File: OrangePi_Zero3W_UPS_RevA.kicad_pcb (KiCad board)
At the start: 4 copper layers, 65 x 32 mm, 74 parts, among them J1 ORANGE_PI_ZERO_3W_HEADER, J2 BATTERY_1S_PROTECTED_NTC, J3 USB_C_POWER_INPUT, Q1 STL9P3LLH6, SW1 POWER / QON, U1 MAX17048G_T10, U2 BQ25895RTWR, U3 STUSB4500LQTR, U4 USBLC6-2SC6, U5 TPS61088RHLR, U6 TPS259470ARPWR

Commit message: Phase 6B.2B5: finalize placement clearance and assembly review
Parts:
- moved C26 0.20 mm to (114.0, 87.5)
- moved C8 0.20 mm to (73.0, 82.8)
- moved Q1 0.20 mm to (76.1, 82.0)
- moved R11 0.20 mm to (76.2, 90.1)
- moved R14 0.20 mm to (106.9, 95.8)
- moved C29 0.15 mm to (117.8, 90.7)
- moved R12 0.15 mm to (77.9, 90.1)
- moved U6 0.15 mm to (117.2, 87.5)
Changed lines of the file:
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@@
 	(footprint "Capacitor_SMD:C_0603_1608Metric"
 		(layer "F.Cu")
-		(at 73.200 82.800 90)
+		(at 73.000 82.800 90)
 		(descr "Capacitor SMD 0603 (1608 Metric), square (rectangular) end terminal, IPC-7351 nominal, (Body size source: IPC-SM-782 page 76, https://www.pcb-3d.com/wordpress/wp-content/uploads/ipc-sm-782a_amendment_1_and_2.pdf), generated with kicad-footprint-generator")
 		(tags "capacitor")
@@
 	(footprint "Resistor_SMD:R_0603_1608Metric"
 		(layer "F.Cu")
-		(at 76.000 90.100 90)
+		(at 76.200 90.100 90)
 		(descr "Resistor SMD 0603 (1608 Metric), square (rectangular) end terminal, IPC-7351 nominal, (Body size source: IPC-SM-782 page 72, https://www.pcb-3d.com/wordpress/wp-content/uploads/ipc-sm-782a_amendment_1_and_2.pdf), generated with kicad-footprint-generator")
 		(tags "resistor")
@@
 	(footprint "Resistor_SMD:R_0603_1608Metric"
 		(layer "F.Cu")
-		(at 77.750 90.100 90)
+		(at 77.900 90.100 90)
 		(descr "Resistor SMD 0603 (1608 Metric), square (rectangular) end terminal, IPC-7351 nominal, (Body size source: IPC-SM-782 page 72, https://www.pcb-3d.com/wordpress/wp-content/uploads/ipc-sm-782a_amendment_1_and_2.pdf), generated with kicad-footprint-generator")
 		(tags "resistor")
@@
 	(footprint "Resistor_SMD:R_0603_1608Metric"
 		(layer "F.Cu")
-		(at 106.900 96.000 -90)
+		(at 106.900 95.800 -90)
 		(descr "Resistor SMD 0603 (1608 Metric), square (rectangular) end terminal, IPC-7351 nominal, (Body size source: IPC-SM-782 page 72, https://www.pcb-3d.com/wordpress/wp-content/uploads/ipc-sm-782a_amendment_1_and_2.pdf), generated with kicad-footprint-generator")
 		(tags "resistor")
@@
 	(footprint "Capacitor_SMD:C_0603_1608Metric"
 		(layer "F.Cu")
-		(at 117.900 90.700 90)
+		(at 117.750 90.700 90)
 		(descr "Capacitor SMD 0603 (1608 Metric), square (rectangular) end terminal, IPC-7351 nominal, (Body size source: IPC-SM-782 page 76, https://www.pcb-3d.com/wordpress/wp-content/uploads/ipc-sm-782a_amendment_1_and_2.pdf), generated with kicad-footprint-generator")
 		(tags "capacitor")
@@
 	(footprint "STL9P3LLH6:TRANS_STL9P3LLH6"
 		(layer "F.Cu")
-		(at 76.300 82.000)
+		(at 76.100 82.000)
 		(property "Reference" "Q1"
 			(at 0 -2.45 0)
@@
 	(footprint "TPS25947_fixed:TPS259470ARPWR_RPW0010A"
 		(layer "F.Cu")
-		(at 117.350 87.500)
+		(at 117.200 87.500)
 		(descr "Texas Instruments RPW0010A VQFN-HR-10, 2.0x2.0mm, 0.45mm pitch; corner terminals use duplicate same-number pad primitives to form the recommended L-shaped lands")
 		(tags "TPS25947 RPW0010A VQFN-HR-10 eFuse")
@@
 	(footprint "Capacitor_SMD:C_0603_1608Metric"
 		(layer "F.Cu")
-		(at 114.200 87.500)
+		(at 114.000 87.500)
 		(descr "Capacitor SMD 0603 (1608 Metric), square (rectangular) end terminal, IPC-7351 nominal, (Body size source: IPC-SM-782 page 76, https://www.pcb-3d.com/wordpress/wp-content/uploads/ipc-sm-782a_amendment_1_and_2.pdf), generated with kicad-footprint-generator")
 		(tags "capacitor")

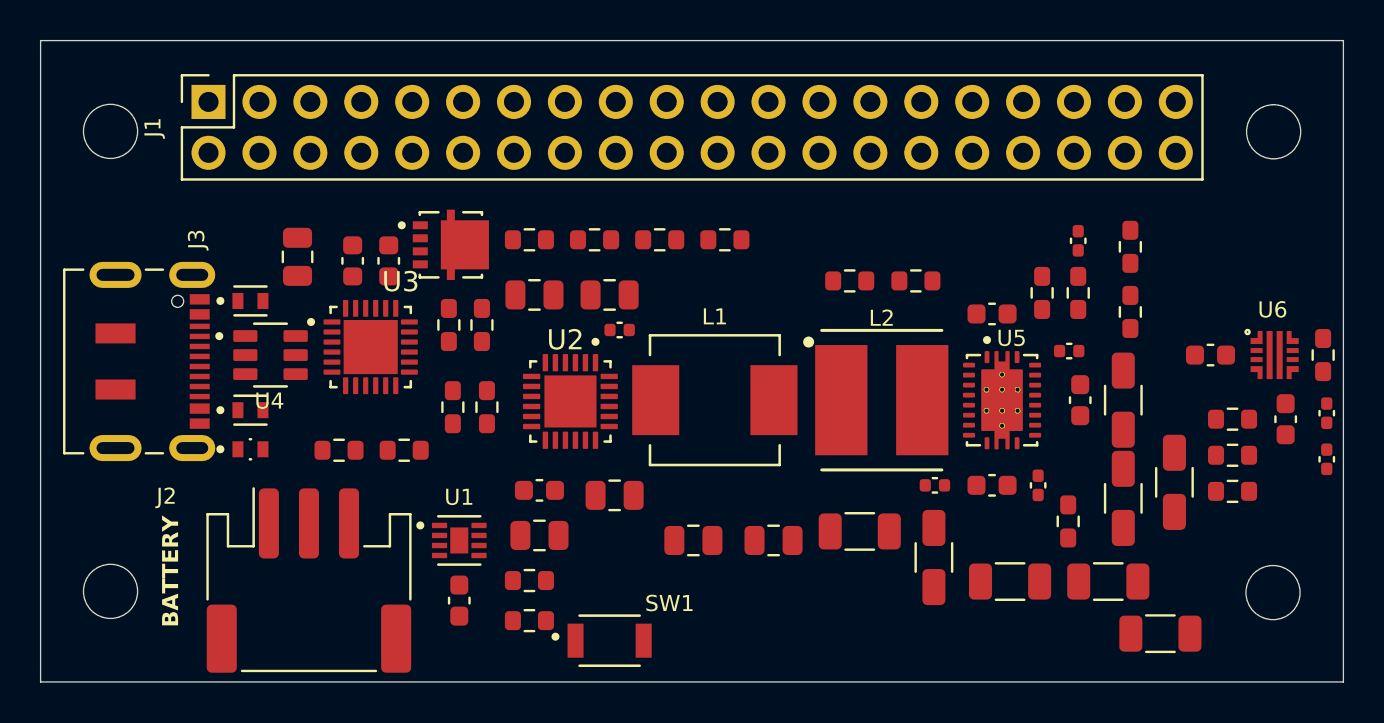
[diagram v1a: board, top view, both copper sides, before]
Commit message: Phase 6B.2B2 — TPS61088, Phase 6B.2B3 — TPS25947, Phase 6B.2B4 — USB-C/STUSB4500L/ESD, Phase 6B.2B5 — final placement review
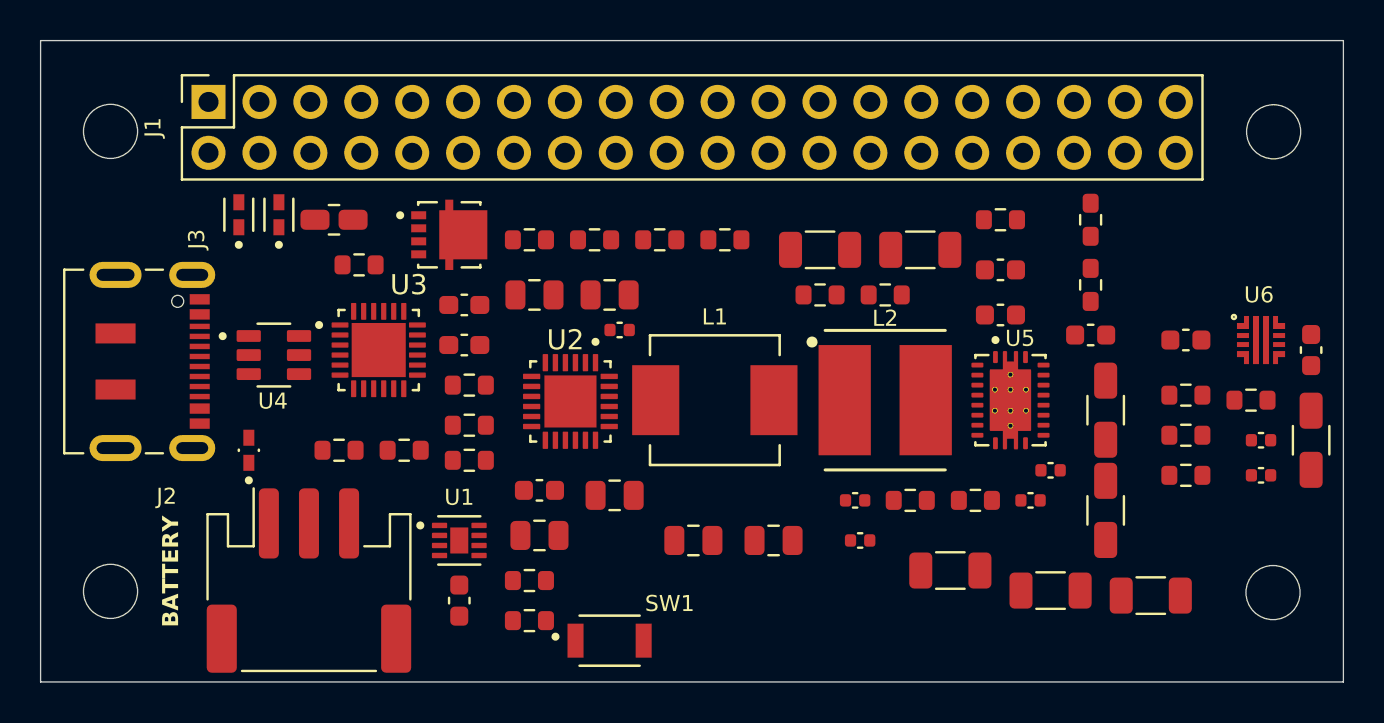
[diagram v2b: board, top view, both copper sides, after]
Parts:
- moved C15 15.4 mm to (99.5, 82.2), turned to 0 degrees
- moved R14 14.5 mm to (97.8, 84.5), turned to 0 degrees
- moved C14 14.2 mm to (94.5, 82.2)
- moved C24 13.2 mm to (105.0, 94.8), turned to 0 degrees
- moved R18 12.3 mm to (99.0, 94.8), turned to 0 degrees
- moved R19 11.6 mm to (102.3, 94.8), turned to 0 degrees
- moved C13 10.8 mm to (103.5, 83.2)
- moved D2 9.85 mm to (67.5, 80.5), turned to 90 degrees
- moved C23 9.30 mm to (96.5, 96.8), turned to 0 degrees
- moved C30 7.14 mm to (119.0, 91.8)
- moved C9 6.98 mm to (76.8, 87.0), turned to 0 degrees
- moved C25 6.02 mm to (106.0, 93.2), turned to 0 degrees
- moved R10 5.39 mm to (71.5, 83.0), turned to 0 degrees
- moved R17 5.21 mm to (103.5, 80.8)
- moved C8 4.36 mm to (76.8, 85.0), turned to 0 degrees
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
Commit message: Phase 6C.1B — Node SYS_BAT lokal
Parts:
- moved C4 2.46 mm to (90.2, 95.2), turned to -90 degrees
- moved C3 1.56 mm to (88.0, 95.2), turned to -90 degrees
- moved C7 0.50 mm to (84.3, 95.0)
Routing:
- net /SYS_BAT: track 0.00 -> 18.9 mm
- net /SW_CHG: track 0.00 -> 4.14 mm
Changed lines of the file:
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@@
 	(footprint "Capacitor_SMD:C_0805_2012Metric"
 		(layer "F.Cu")
-		(at 84.27 94.5)
+		(at 84.27 95)
 		(descr "Capacitor SMD 0805 (2012 Metric), square (rectangular) end terminal, IPC-7351 nominal, (Body size source: IPC-SM-782 page 76, https://www.pcb-3d.com/wordpress/wp-content/uploads/ipc-sm-782a_amendment_1_and_2.pdf, https://docs.google.com/spreadsheets/d/1BsfQQcO9C6DZCsRaXUlFlo91Tg2WpOkGARC1WS5S8t0/edit?usp=sharing), generated with kicad-footprint-generator")
 		(tags "capacitor")
@@
 	(footprint "Capacitor_SMD:C_0805_2012Metric"
 		(layer "F.Cu")
-		(at 92.2 96.75)
+		(at 90.25 95.25 -90)
 		(descr "Capacitor SMD 0805 (2012 Metric), square (rectangular) end terminal, IPC-7351 nominal, (Body size source: IPC-SM-782 page 76, https://www.pcb-3d.com/wordpress/wp-content/uploads/ipc-sm-782a_amendment_1_and_2.pdf, https://docs.google.com/spreadsheets/d/1BsfQQcO9C6DZCsRaXUlFlo91Tg2WpOkGARC1WS5S8t0/edit?usp=sharing), generated with kicad-footprint-generator")
 		(tags "capacitor")
 		(property "Reference" "C4"
-			(at 0 -1.5 0)
+			(at 0 -1.5 90)
 			(layer "F.SilkS")
 			(hide yes)
@@
 		)
 		(property "Value" "10uF"
-			(at 0 1.68 0)
+			(at 0 1.68 90)
 			(layer "F.Fab")
 			(effects
@@
 		)
 		(property "Datasheet" "~"
-			(at 0 0 0)
+			(at 0 0 90)
 			(layer "F.Fab")
 			(hide yes)
@@
 		)
 		(property "Description" "Unpolarized capacitor"
-			(at 0 0 0)
+			(at 0 0 90)
 			(layer "F.Fab")
 			(hide yes)
@@
 		(attr smd)
 		(fp_line
-			(start -0.261252 -0.735)
-			(end 0.261252 -0.735)
+			(start -0.261252 0.735)
+			(end 0.261252 0.735)
 			(stroke
 				(width 0.12)
@@
 		)
 		(fp_line
-			(start -0.261252 0.735)
-			(end 0.261252 0.735)
+			(start -0.261252 -0.735)
+			(end 0.261252 -0.735)
 			(stroke
 				(width 0.12)
@@
 		)
 		(fp_line
-			(start -1.7 -0.98)
-			(end 1.7 -0.98)
+			(start -1.7 0.98)
+			(end -1.7 -0.98)
 			(stroke
 				(width 0.05)
@@
 		)
 		(fp_line
-			(start -1.7 0.98)
-			(end -1.7 -0.98)
+			(start 1.7 0.98)
+			(end -1.7 0.98)
 			(stroke
 				(width 0.05)
@@
 		)
 		(fp_line
-			(start 1.7 -0.98)
-			(end 1.7 0.98)
+			(start -1.7 -0.98)
+			(end 1.7 -0.98)
 			(stroke
 				(width 0.05)
@@
 		)
 		(fp_line
-			(start 1.7 0.98)
-			(end -1.7 0.98)
+			(start 1.7 -0.98)
+			(end 1.7 0.98)
 			(stroke
 				(width 0.05)
@@
 		)
 		(fp_line
-			(start -1 -0.625)
-			(end 1 -0.625)
+			(start -1 0.625)
+			(end -1 -0.625)
 			(stroke
 				(width 0.1)
@@
 		)
 		(fp_line
-			(start -1 0.625)
-			(end -1 -0.625)
+			(start 1 0.625)
+			(end -1 0.625)
 			(stroke
 				(width 0.1)
@@
 		)
 		(fp_line
-			(start 1 -0.625)
-			(end 1 0.625)
+			(start -1 -0.625)
+			(end 1 -0.625)
 			(stroke
 				(width 0.1)
@@
 		)
 		(fp_line
-			(start 1 0.625)
-			(end -1 0.625)
+			(start 1 -0.625)
+			(end 1 0.625)
 			(stroke
 				(width 0.1)
@@
 		)
 		(fp_text user "${REFERENCE}"
-			(at 0 0 0)
+			(at 0 0 90)
 			(layer "F.Fab")
 			(effects
@@
 		)
 		(pad "1" smd roundrect
-			(at -0.95 0)
+			(at -0.95 0 270)
 			(size 1 1.45)
 			(layers "F.Cu" "F.Mask" "F.Paste")
@@
 		)
 		(pad "2" smd roundrect
-			(at 0.95 0)
+			(at 0.95 0 270)
 			(size 1 1.45)
 			(layers "F.Cu" "F.Mask" "F.Paste")
@@
 	(footprint "Capacitor_SMD:C_0805_2012Metric"
 		(layer "F.Cu")
-		(at 88.2 96.75)
+		(at 88.05 95.2 -90)
 		(descr "Capacitor SMD 0805 (2012 Metric), square (rectangular) end terminal, IPC-7351 nominal, (Body size source: IPC-SM-782 page 76, https://www.pcb-3d.com/wordpress/wp-content/uploads/ipc-sm-782a_amendment_1_and_2.pdf, https://docs.google.com/spreadsheets/d/1BsfQQcO9C6DZCsRaXUlFlo91Tg2WpOkGARC1WS5S8t0/edit?usp=sharing), generated with kicad-footprint-generator")
 		(tags "capacitor")
 		(property "Reference" "C3"
-			(at 0 -1.5 0)
+			(at 0 -1.5 90)
 			(layer "F.SilkS")
 			(hide yes)
@@
 		)
 		(property "Value" "10uF"
-			(at 0 1.68 0)
+			(at 0 1.68 90)
 			(layer "F.Fab")
 			(effects
@@
 		)
 		(property "Datasheet" "~"
-			(at 0 0 0)
+			(at 0 0 90)
 			(layer "F.Fab")
 			(hide yes)
@@
 		)
 		(property "Description" "Unpolarized capacitor"
-			(at 0 0 0)
+			(at 0 0 90)
 			(layer "F.Fab")
 			(hide yes)
@@
 		(attr smd)
 		(fp_line
-			(start -0.261252 -0.735)
-			(end 0.261252 -0.735)
+			(start -0.261252 0.735)
+			(end 0.261252 0.735)
 			(stroke
 				(width 0.12)
@@
 		)
 		(fp_line
-			(start -0.261252 0.735)
-			(end 0.261252 0.735)
+			(start -0.261252 -0.735)
+			(end 0.261252 -0.735)
 			(stroke
 				(width 0.12)
@@
 		)
 		(fp_line
-			(start -1.7 -0.98)
-			(end 1.7 -0.98)
+			(start -1.7 0.98)
+			(end -1.7 -0.98)
 			(stroke
 				(width 0.05)
@@
 		)
 		(fp_line
-			(start -1.7 0.98)
-			(end -1.7 -0.98)
+			(start 1.7 0.98)
+			(end -1.7 0.98)
 			(stroke
 				(width 0.05)
@@
 		)
 		(fp_line
-			(start 1.7 -0.98)
-			(end 1.7 0.98)
+			(start -1.7 -0.98)
+			(end 1.7 -0.98)
 			(stroke
 				(width 0.05)
@@
 		)
 		(fp_line
-			(start 1.7 0.98)
-			(end -1.7 0.98)
+			(start 1.7 -0.98)
+			(end 1.7 0.98)
 			(stroke
 				(width 0.05)
@@
 		)
 		(fp_line
-			(start -1 -0.625)
-			(end 1 -0.625)
+			(start -1 0.625)
+			(end -1 -0.625)
 			(stroke
 				(width 0.1)
@@
 		)
 		(fp_line
-			(start -1 0.625)
-			(end -1 -0.625)
+			(start 1 0.625)
+			(end -1 0.625)
 			(stroke
 				(width 0.1)
@@
 		)
 		(fp_line
-			(start 1 -0.625)
-			(end 1 0.625)
+			(start -1 -0.625)
+			(end 1 -0.625)
 			(stroke
 				(width 0.1)
@@
 		)
 		(fp_line
-			(start 1 0.625)
-			(end -1 0.625)
+			(start 1 -0.625)
+			(end 1 0.625)
 			(stroke
 				(width 0.1)
@@
 		)
 		(fp_text user "${REFERENCE}"
-			(at 0 0 0)
+			(at 0 0 90)
 			(layer "F.Fab")
 			(effects
@@
 		)
 		(pad "1" smd roundrect
-			(at -0.95 0)
+			(at -0.95 0 270)
 			(size 1 1.45)
 			(layers "F.Cu" "F.Mask" "F.Paste")
@@
 		)
 		(pad "2" smd roundrect
-			(at 0.95 0)
+			(at 0.95 0 270)
 			(size 1 1.45)
 			(layers "F.Cu" "F.Mask" "F.Paste")
@@
 		)
 	)
+	(segment
+		(start 88.05 94.25)
+		(end 86.925 93.125)
+		(width 0.8)
+		(layer "F.Cu")
+		(net 35)
+	)
+	(segment
+		(start 82.315 92.315)
+		(end 82.315 91.75)
+		(width 0.3)
+		(layer "F.Cu")
+		(net 35)
+	)
+	(segment
+		(start 92 92.55)
+		(end 92 89.97)
+		(width 1.2)
+		(layer "F.Cu")
+		(net 35)
+	)
+	(segment
+		(start 86.925 93.125)
+		(end 82.625 93.125)
+		(width 0.8)
+		(layer "F.Cu")
+		(net 35)
+	)
+	(segment
+		(start 81.815 92.315)
+		(end 81.815 91.75)
+		(width 0.3)
+		(layer "F.Cu")
+		(net 35)
+	)
+	(segment
+		(start 82.874 93.374)
+		(end 82.625 93.125)
+		(width 0.3)
+		(layer "F.Cu")
+		(net 35)
+	)
+	(segment
+		(start 90.25 94.3)
+		(end 92 92.55)
+		(width 1.2)
+		(layer "F.Cu")
+		(net 35)
+	)
+	(segment
+		(start 83.74924 92.924)
+		(end 82.924 92.924)
+		(width 0.3)
+		(layer "F.Cu")
+		(net 35)
+	)
+	(segment
+		(start 83.29924 93.374)
+		(end 82.874 93.374)
+		(width 0.3)
+		(layer "F.Cu")
+		(net 35)
+	)
+	(segment
+		(start 82.625 93.125)
+		(end 81.815 92.315)
+		(width 0.3)
+		(layer "F.Cu")
+		(net 35)
+	)
+	(segment
+		(start 92 89.97)
+		(end 92.22 89.75)
+		(width 1.2)
+		(layer "F.Cu")
+		(net 35)
+	)
+	(segment
+		(start 90.2 94.25)
+		(end 90.25 94.3)
+		(width 0.8)
+		(layer "F.Cu")
+		(net 35)
+	)
+	(segment
+		(start 82.924 92.924)
+		(end 82.315 92.315)
+		(width 0.3)
+		(layer "F.Cu")
+		(net 35)
+	)
+	(segment
+		(start 83.74924 92.924)
+		(end 83.29924 93.374)
+		(width 0.3)
+		(layer "F.Cu")
+		(net 35)
+	)
+	(segment
+		(start 88.05 94.25)
+		(end 90.2 94.25)
+		(width 0.8)
+		(layer "F.Cu")
+		(net 35)
+	)
+	(segment
+		(start 84 91.065)
+		(end 85.005 91.065)
+		(width 0.3)
+		(layer "F.Cu")
+		(net 37)
+	)
+	(segment
+		(start 85.119 90.951)
+		(end 86.32 89.75)
+		(width 1.2)
+		(layer "F.Cu")
+		(net 37)
+	)
+	(segment
+		(start 84.733 90.565)
+		(end 85.119 90.951)
+		(width 0.3)
+		(layer "F.Cu")
+		(net 37)
+	)
+	(segment
+		(start 84 90.565)
+		(end 84.733 90.565)
+		(width 0.3)
+		(layer "F.Cu")
+		(net 37)
+	)
+	(segment
+		(start 85.005 91.065)
+		(end 85.119 90.951)
+		(width 0.3)
+		(layer "F.Cu")
+		(net 37)
+	)
 	(zone

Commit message: Phase 6C.1C — BQ25895 local PGND return
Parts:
- moved C7 0.27 mm to (84.0, 95.0)
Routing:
- net GND: track 0.00 -> 20.1 mm, vias 0 -> 6
- net /SYS_BAT: track 18.9 -> 24.8 mm
- net /SW_CHG: track 4.14 -> 6.68 mm
